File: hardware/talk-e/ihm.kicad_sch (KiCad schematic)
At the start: 28 parts, among them J1 Conn_01x04_Socket, J2 Conn_01x02_Socket, J3 Conn_02x04_Odd_Even, Q2 BC337, SW1 SW_Push, SW2 SW_Push, SW3 SW_Push, SW5 SW_Push, U1 RFM96W-433S2, U4 ESP32-S3

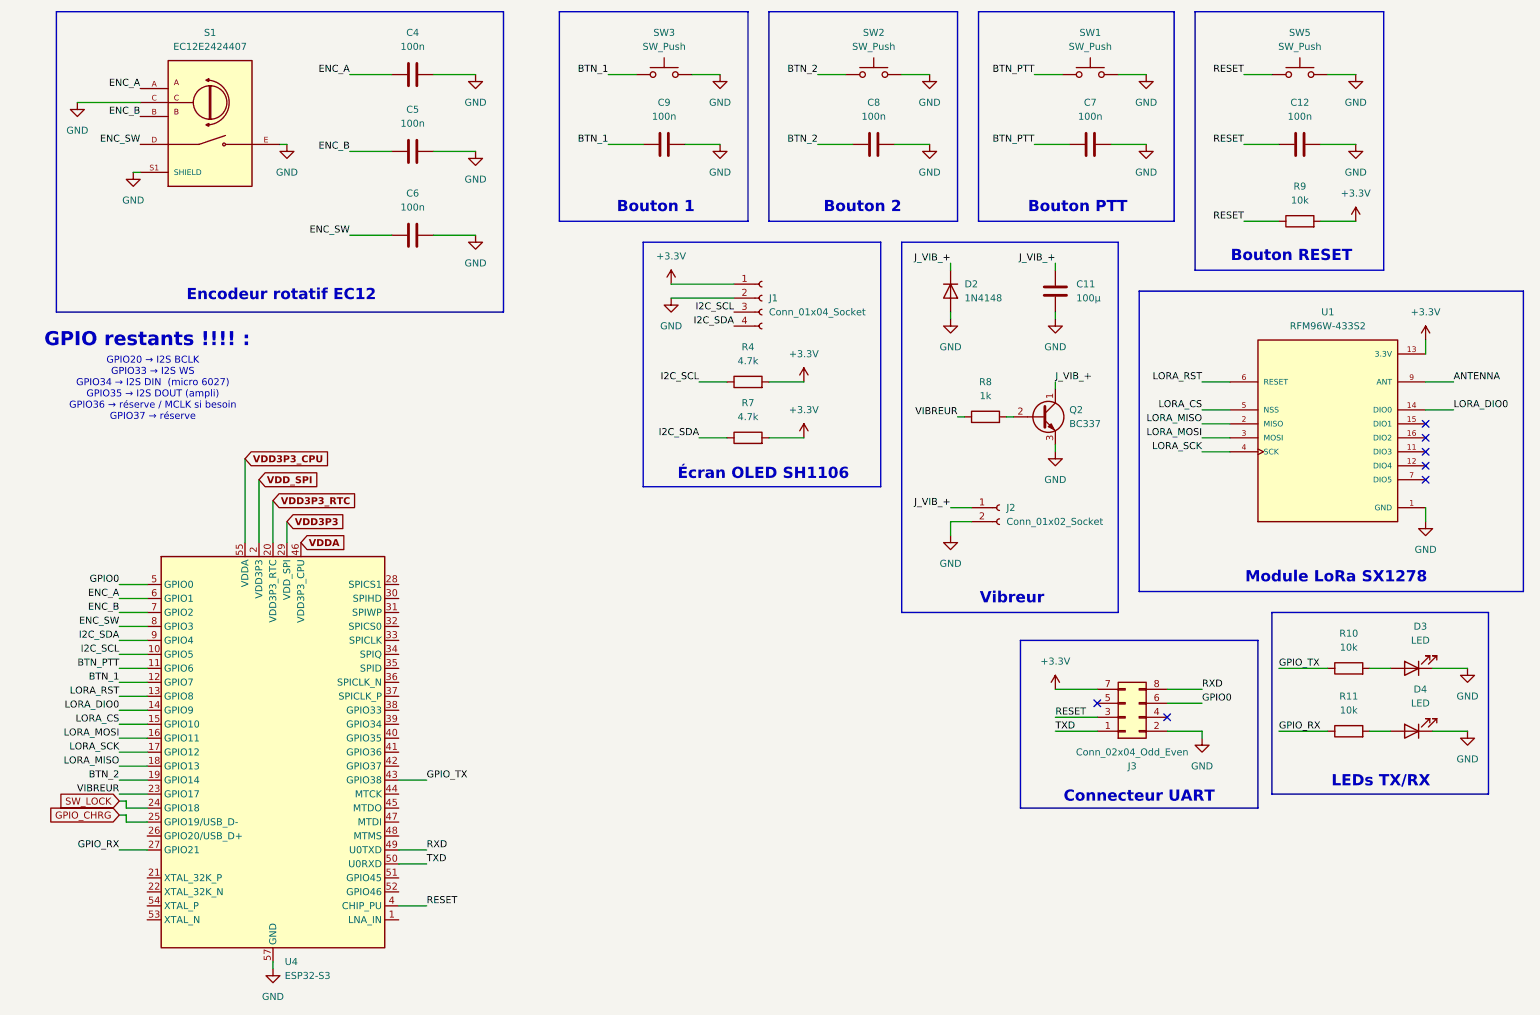
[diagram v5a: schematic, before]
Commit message: Added SMA connector (antenna)
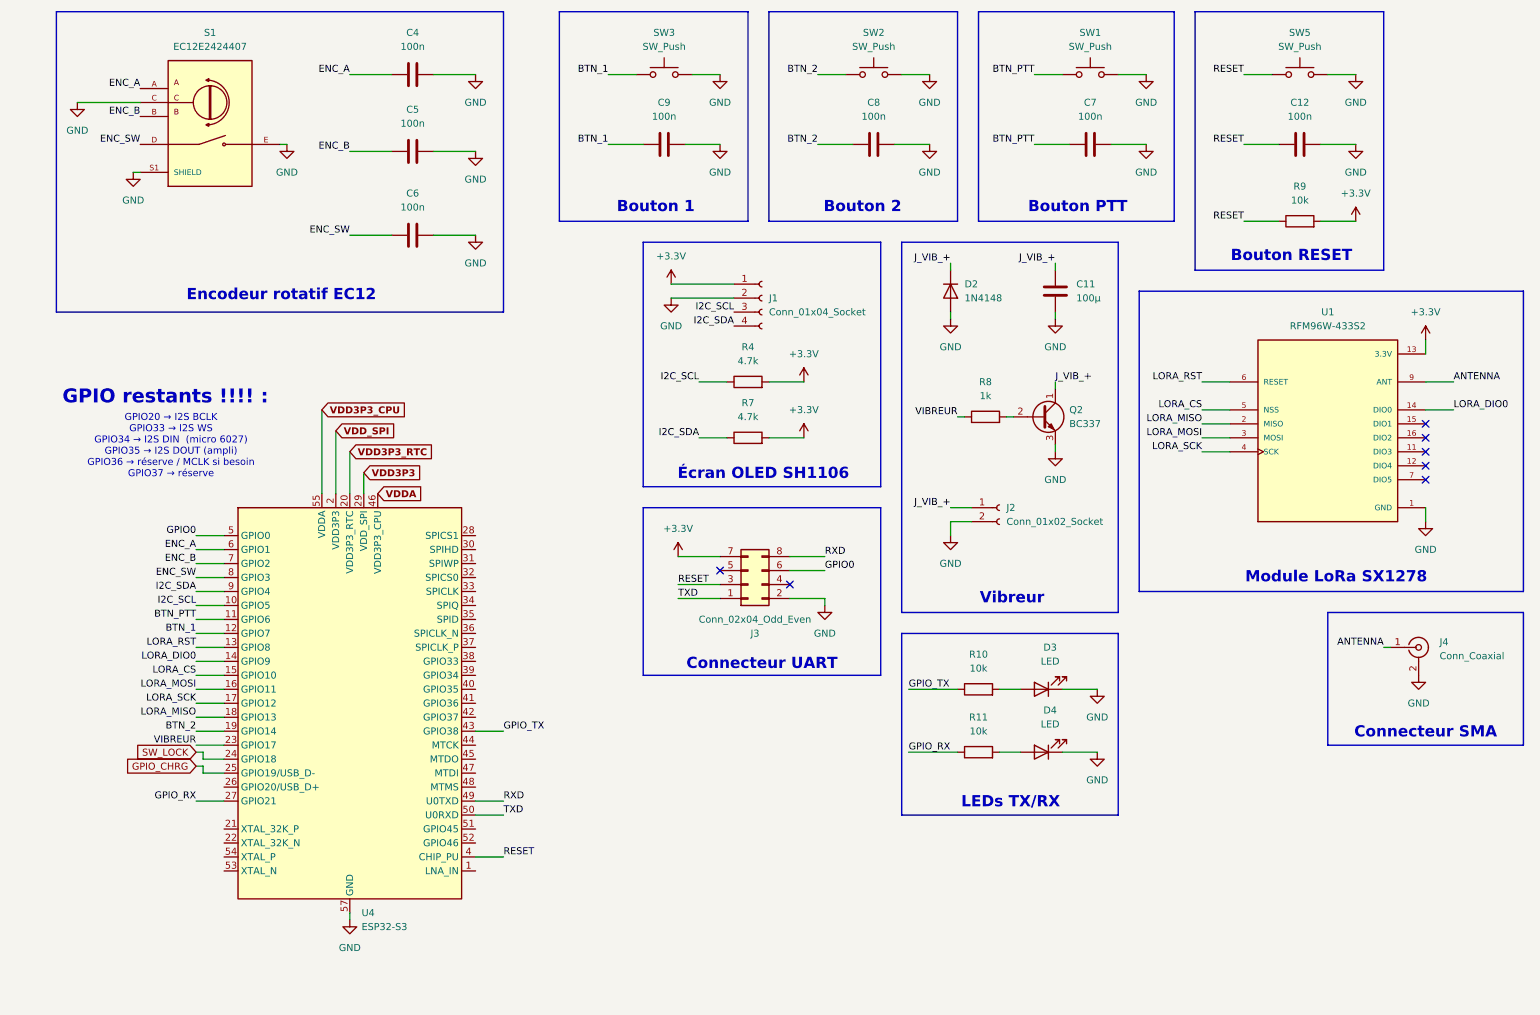
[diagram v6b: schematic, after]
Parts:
- added J4: Conn_Coaxial, Connector_Coaxial:SMA_Amphenol_901-143_Horizontal, symbol Connector:Conn_Coaxial
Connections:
- net ANTENNA: now also J4.1 (In)
- net GND: now also J4.2 (Ext)
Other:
- note added: "Connecteur SMA"
- moved on the sheet: D3, D4, J3, R10, R11, U4

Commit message: Added crystal
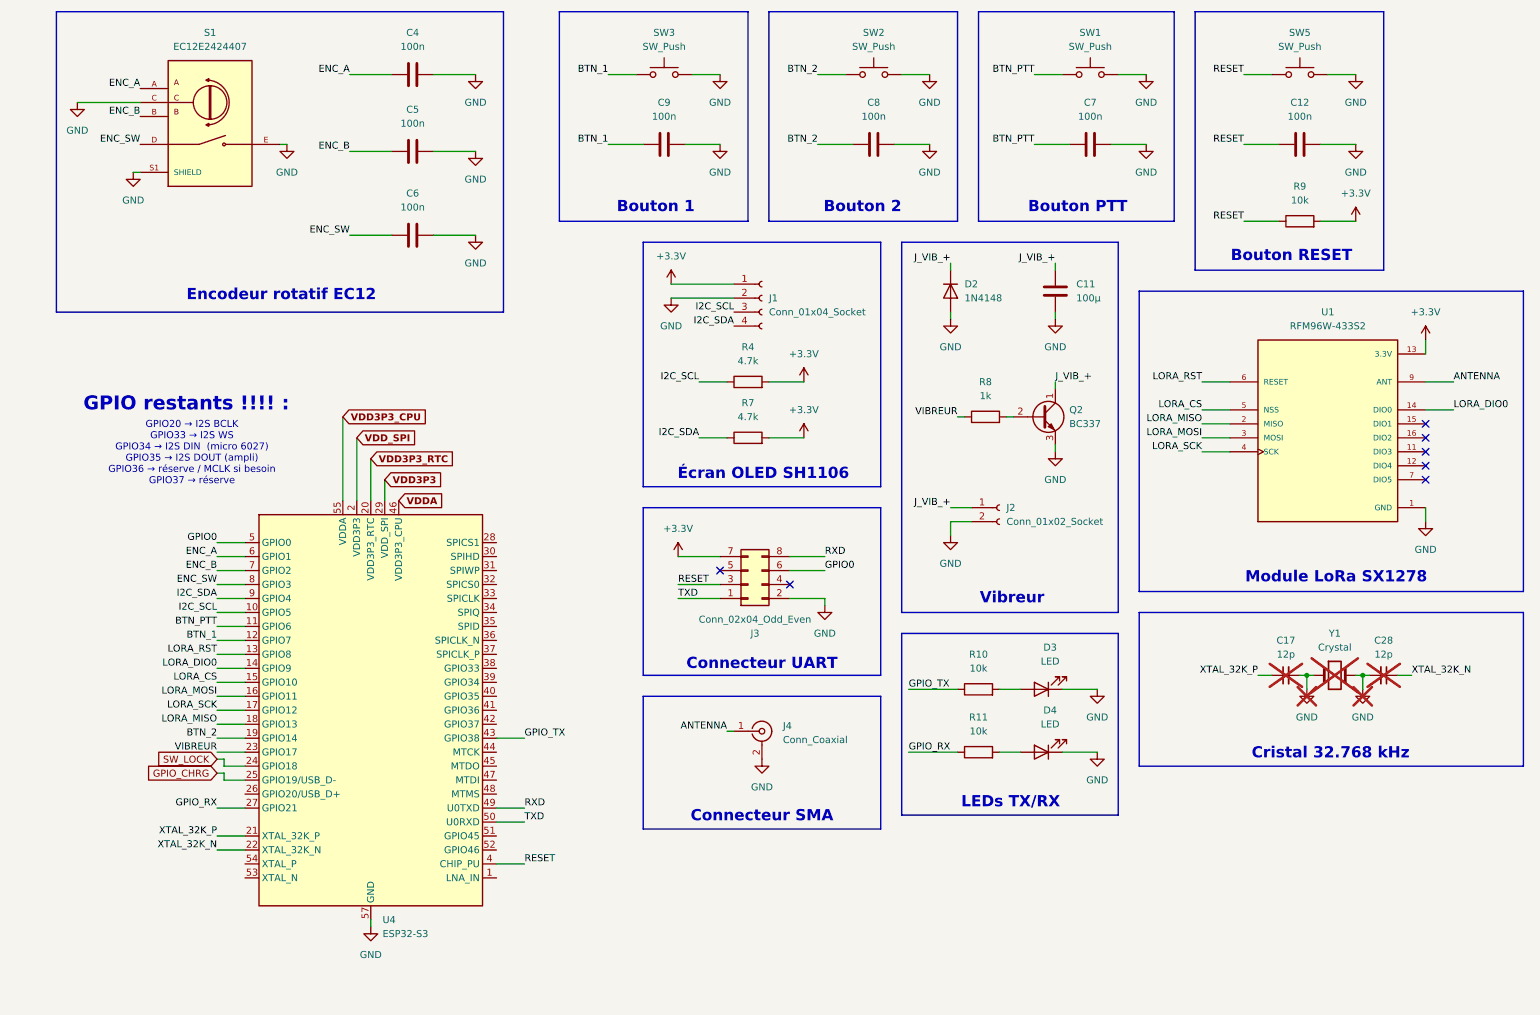
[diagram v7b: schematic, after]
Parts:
- added C17, C28: 12p, symbol Device:C_Small
- added Y1: Crystal, symbol Device:Crystal
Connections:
- net GND: now also C17.2, C28.2, Y1.1, Y1.2
- net XTAL_32K_P: now reaches U4.21 (XTAL_32K_P)
- net XTAL_32K_P: now also C17.1
- net XTAL_32K_N: now reaches U4.22 (XTAL_32K_N)
- net XTAL_32K_N: now also C28.1
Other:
- note added: "Cristal 32.768 kHz"
- moved on the sheet: J4, U4

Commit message: Something moved in the schematic but idk what
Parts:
- removed C12: 100n, symbol Device:C
- removed R9: 10k, symbol Device:R
- removed SW5: SW_Push, symbol Switch:SW_Push
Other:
- note removed: "Bouton RESET"
- moved on the sheet: J1, J3, J4, R4, R7, U4
